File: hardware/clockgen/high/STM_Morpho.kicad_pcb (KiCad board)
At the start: 4 copper layers, 70 x 95.8 mm, 32 parts, among them CN10 Conn_02x19_Odd_Even, CN7 Conn_02x19_Odd_Even, J1 Conn_02x20_Odd_Even, J2 Conn_02x20_Odd_Even, U1 74ALVC164245DLG4, U10 CD40109BNSR, U2 74ALVC164245DLG4, U3 CD40109BNSR, U4 CD40109BNSR, U5 CD40109BNSR, U6 CD40109BNSR, U7 CD40109BNSR, U8 CD40109BNSR, U9 CD40109BNSR

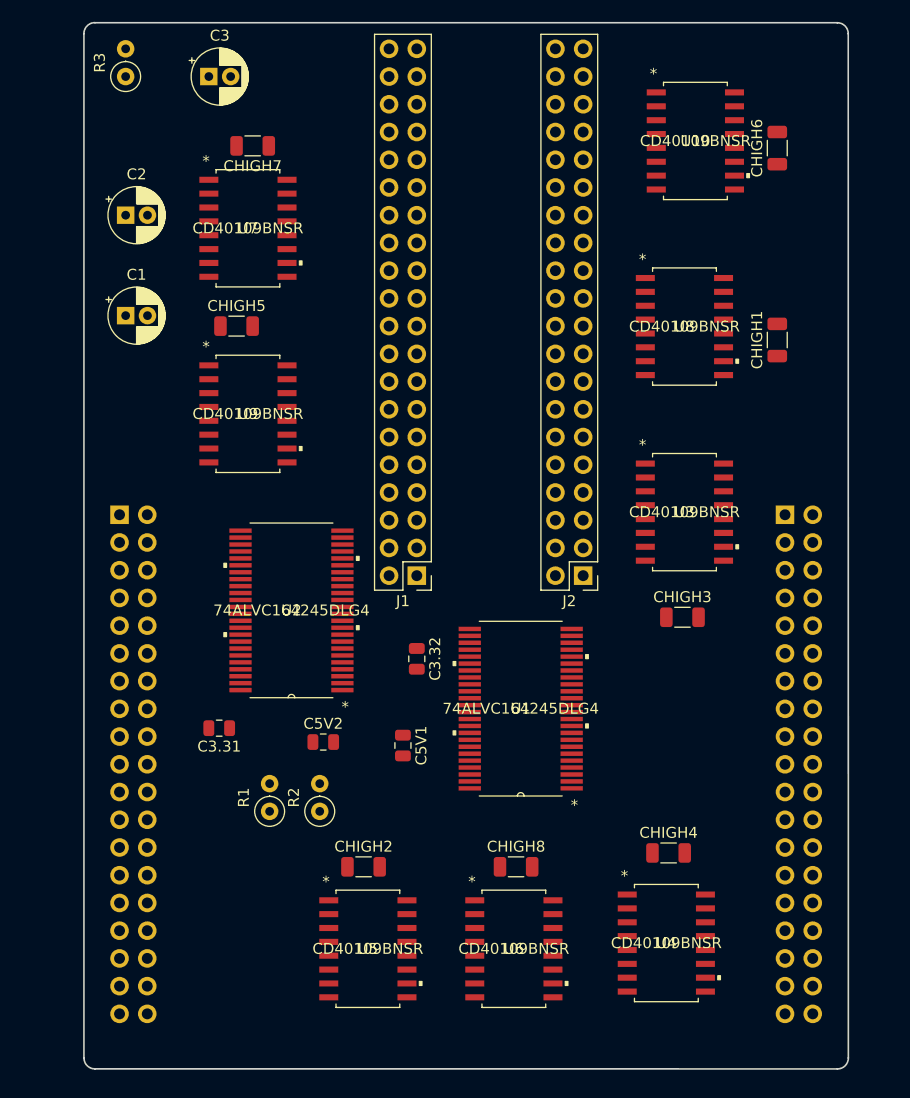
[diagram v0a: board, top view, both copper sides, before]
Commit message: Two PCBs are routed
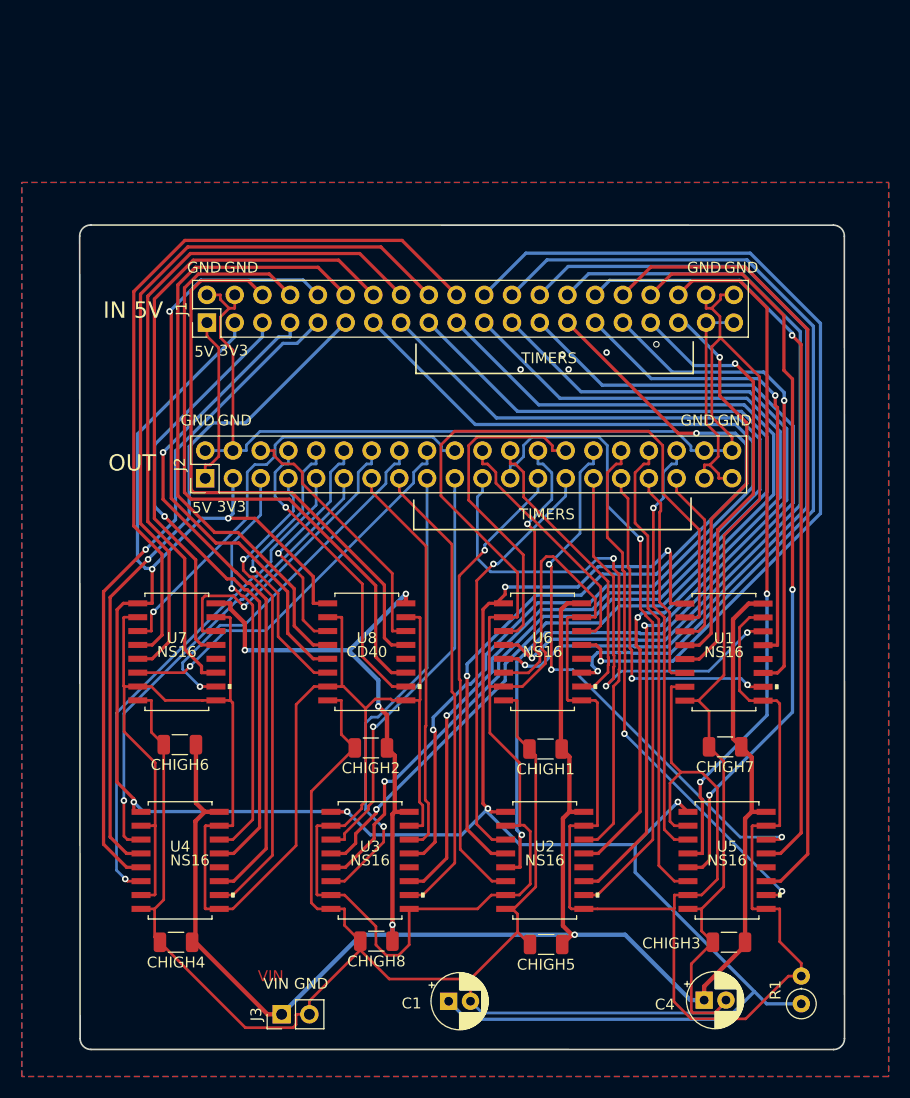
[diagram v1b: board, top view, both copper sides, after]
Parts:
- removed C2, C3: CP, Capacitor_THT:CP_Radial_D5.0mm_P2.00mm
- removed C3.31, C3.32, C5V1, C5V2: C, Capacitor_SMD:C_0805_2012Metric
- removed CN10, CN7: Conn_02x19_Odd_Even, Connector_PinSocket_2.54mm:PinSocket_2x19_P2.54mm_Vertical
- removed R2: 10K, Resistor_THT:R_Axial_DIN0207_L6.3mm_D2.5mm_P2.54mm_Vertical
- removed R3: 1K, Resistor_THT:R_Axial_DIN0207_L6.3mm_D2.5mm_P2.54mm_Vertical
- removed U10, U9: CD40109BNSR, CD40109BNSR:CD40109BNSR
- added C4: CP, Capacitor_THT:CP_Radial_D5.0mm_P2.00mm, F.Cu at (186.8, 115.7)
- added J3: Conn_01x02_Female, Connector_PinHeader_2.54mm:PinHeader_1x02_P2.54mm_Vertical, F.Cu at (148.1, 117.0)
- R1: value 10K -> 1K
- U1, U2: value 74ALVC164245DLG4 -> NS16; footprint footprints:74ALVC164245DLG4 -> CD40109BNSR:CD40109BNSR
- U3, U4, U5, U6, U7: value CD40109BNSR -> NS16
- U8: value CD40109BNSR -> CD40
- moved CHIGH6 77.3 mm to (138.8, 92.3), turned to 180 degrees
- moved CHIGH7 70.0 mm to (188.7, 92.5)
- moved C1 69.4 mm to (163.4, 115.8)
- moved CHIGH5 63.3 mm to (172.3, 110.6), turned to 180 degrees
- moved R1 51.8 mm to (195.7, 116.0)
- moved CHIGH4 45.9 mm to (138.4, 110.4), turned to 180 degrees
- moved U4 45.2 mm to (138.8, 102.9)
- moved CHIGH1 43.1 mm to (172.3, 92.7), turned to 180 degrees
- moved U3 43.0 mm to (156.2, 102.9)
- moved U8 41.7 mm to (155.9, 83.8)
- moved U7 39.3 mm to (138.5, 83.8)
- moved J2 35.8 mm to (141.1, 67.9), turned to 90 degrees
- moved U5 33.9 mm to (188.9, 102.9)
- moved U2 32.6 mm to (172.2, 102.9), turned to 0 degrees
- moved J1 30.1 mm to (141.3, 53.6), turned to 90 degrees
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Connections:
- C1 pad 1: +5V -> +3V3
- J1 pad 1: +5V -> /+5V
- J1 pad 10: /PB9_5V -> /PC8_HIGH
- J1 pad 11: /PA6_5V -> /PA3_HIGH
- J1 pad 12: /PA7_5V -> /PC6_HIGH
- J1 pad 13: /PA1_5V -> /PA2_HIGH
- J1 pad 14: /PA2_5V -> /PC5_HIGH
- J1 pad 15: /PA3_5V -> /PA1_HIGH
- J1 pad 16: /PA4_5V -> /PC4_HIGH
- J1 pad 17: /PA5_5V -> /PA7_HIGH
- J1 pad 18: /PA8_5V -> /PC3_HIGH
- J1 pad 19: /NC -> /PA6_HIGH
- J1 pad 2: +3V3 -> GND
- J1 pad 20: /NC -> /PC2_HIGH
- J1 pad 21: GND -> /PB9_HIGH
- J1 pad 22: GND -> /PC1_HIGH
- J1 pad 23: /PA9_5V -> /PB8_HIGH
- J1 pad 24: /PA11_5V -> /PC0_HIGH
- J1 pad 25: /PA12_5V -> /PC7_HIGH
- J1 pad 26: /PA13_5V -> /PA15_HIGH
- J1 pad 27: /PA14_5V -> /PA0_HIGH
- J1 pad 28: /PA15_5V -> /PA14_HIGH
- J1 pad 29: /PC0_5V -> /PB6_HIGH
- J1 pad 3: /PA10_5V -> +3V3
- J1 pad 30: /PC1_5V -> /PA13_HIGH
- J1 pad 31: /PC2_5V -> /PB5_HIGH
- J1 pad 32: /PC3_5V -> /PA12_HIGH
- J1 pad 33: /PC4_5V -> /PB10_HIGH
- J1 pad 34: /PC5_5V -> /PA11_HIGH
- J1 pad 35: /PC6_5V -> /PA10_HIGH
- J1 pad 36: /PC8_5V -> /PA9_HIGH
- J1 pad 37: /PC9_5V -> /NC
- J1 pad 38: /PC10_5V -> GND
- J1 pad 39: GND -> /NC
- J1 pad 4: /PB10_5V -> GND
- J1 pad 5: /PB5_5V -> /PA8_HIGH
- J1 pad 6: /PB6_5V -> /PC10_HIGH
- J1 pad 7: /PA0_5V -> /PA5_HIGH
- J1 pad 8: /PC7_5V -> /PC9_HIGH
- J1 pad 9: /PB8_5V -> /PA4_HIGH
- J2 pad 1: +5V -> /+5V
- J2 pad 10: /PB9_HIGH -> /PC8_5V
- J2 pad 11: /PA6_HIGH -> /PA3_5V
- J2 pad 12: /PA7_HIGH -> /PC6_5V
- J2 pad 13: /PA1_HIGH -> /PA2_5V
- J2 pad 14: /PA2_HIGH -> /PC5_5V
- J2 pad 15: /PA3_HIGH -> /PA1_5V
- J2 pad 16: /PA4_HIGH -> /PC4_5V
- J2 pad 17: /PA5_HIGH -> /PA7_5V
- J2 pad 18: /PA8_HIGH -> /PC3_5V
- J2 pad 19: +15V -> /PA6_5V
- J2 pad 2: +3V3 -> GND
- J2 pad 20: +15V -> /PC2_5V
- J2 pad 21: GND -> /PB9_5V
- J2 pad 22: GND -> /PC1_5V
- J2 pad 23: /PA9_HIGH -> /PB8_5V
- J2 pad 24: /PA11_HIGH -> /PC0_5V
- J2 pad 25: /PA12_HIGH -> /PC7_5V
- J2 pad 26: /PA13_HIGH -> /PA15_5V
- J2 pad 27: /PA14_HIGH -> /PA0_5V
- J2 pad 28: /PA15_HIGH -> /PA14_5V
- J2 pad 29: /PC0_HIGH -> /PB6_5V
- J2 pad 3: /PA10_HIGH -> +3V3
- J2 pad 30: /PC1_HIGH -> /PA13_5V
- J2 pad 31: /PC2_HIGH -> /PB5_5V
- J2 pad 32: /PC3_HIGH -> /PA12_5V
- J2 pad 33: /PC4_HIGH -> /PB10_5V
- J2 pad 34: /PC5_HIGH -> /PA11_5V
- J2 pad 35: /PC6_HIGH -> /PA10_5V
- J2 pad 36: /PC8_HIGH -> /PA9_5V
- J2 pad 37: /PC9_HIGH -> /NC
- J2 pad 38: /PC10_HIGH -> GND
- J2 pad 39: GND -> /NC
- J2 pad 4: /PB10_HIGH -> GND
- J2 pad 5: /PB5_HIGH -> /PA8_5V
- J2 pad 6: /PB6_HIGH -> /PC10_5V
- J2 pad 7: /PA0_HIGH -> /PA5_5V
- J2 pad 8: /PC7_HIGH -> /PC9_5V
- J2 pad 9: /PB8_HIGH -> /PA4_5V
- R1 pad 2: /PULLUP -> /PULLUP_HIGH
- U1 pad 1: /PULLUP -> +3V3
- U1 pad 10: GND -> /PB5_5V
- U1 pad 11: /PB8_5V -> /PB5_HIGH
- U1 pad 12: /PB9_5V -> (no net)
- U1 pad 13: /PA6_5V -> /PB6_HIGH
- U1 pad 14: /PA7_5V -> /PB6_5V
- U1 pad 15: GND -> /PULLUP_HIGH
- U1 pad 16: /PA1_5V -> +15V
- U1 pad 2: /PA10_5V -> /PULLUP_HIGH
- U1 pad 3: /PB10_5V -> /PA10_5V
- U1 pad 4: GND -> /PA10_HIGH
- U1 pad 5: /PB5_5V -> /PB10_HIGH
- U1 pad 6: /PB6_5V -> /PB10_5V
- U1 pad 7: +5V -> /PULLUP_HIGH
- U1 pad 8: /PA0_5V -> GND
- U1 pad 9: /PC7_5V -> /PULLUP_HIGH
- U2 pad 1: /PULLUP -> +3V3
- U2 pad 10: GND -> /PB8_5V
- U2 pad 11: /PC0_5V -> /PB8_HIGH
- U2 pad 12: /PC1_5V -> (no net)
- U2 pad 13: /PC2_5V -> /PB9_HIGH
- U2 pad 14: /PC3_5V -> /PB9_5V
- U2 pad 15: GND -> /PULLUP_HIGH
- U2 pad 16: /PC4_5V -> +15V
- U2 pad 2: /PA9_5V -> /PULLUP_HIGH
- U2 pad 3: /PA11_5V -> /PA0_5V
- U2 pad 4: GND -> /PA0_HIGH
- U2 pad 5: /PA12_5V -> /PC7_HIGH
- U2 pad 6: /PA13_5V -> /PC7_5V
- U2 pad 7: +5V -> /PULLUP_HIGH
- U2 pad 8: /PA14_5V -> GND
- U2 pad 9: /PA15_5V -> /PULLUP_HIGH
- U3 pad 10: /PB5 -> /PA1_5V
- U3 pad 11: /PB5_HIGH -> /PA1_HIGH
- U3 pad 13: /PB6_HIGH -> /PA2_HIGH
- U3 pad 14: /PB6 -> /PA2_5V
- U3 pad 3: /PA10 -> /PA6_5V
- U3 pad 4: /PA10_HIGH -> /PA6_HIGH
- U3 pad 5: /PB10_HIGH -> /PA7_HIGH
- U3 pad 6: /PB10 -> /PA7_5V
- U4 pad 10: /PB8 -> /PA5_5V
- U4 pad 11: /PB8_HIGH -> /PA5_HIGH
- U4 pad 13: /PB9_HIGH -> /PA8_HIGH
- U4 pad 14: /PB9 -> /PA8_5V
- U4 pad 3: /PA0 -> /PA3_5V
- U4 pad 4: /PA0_HIGH -> /PA3_HIGH
- U4 pad 5: /PC7_HIGH -> /PA4_HIGH
- U4 pad 6: /PC7 -> /PA4_5V
- U5 pad 10: /PA1 -> /PA12_5V
- U5 pad 11: /PA1_HIGH -> /PA12_HIGH
- U5 pad 13: /PA2_HIGH -> /PA13_HIGH
- U5 pad 14: /PA2 -> /PA13_5V
- U5 pad 3: /PA6 -> /PA9_5V
- U5 pad 4: /PA6_HIGH -> /PA9_HIGH
- U5 pad 5: /PA7_HIGH -> /PA11_HIGH
- U5 pad 6: /PA7 -> /PA11_5V
- U6 pad 10: /PA5 -> /PC0_5V
- U6 pad 11: /PA5_HIGH -> /PC0_HIGH
- U6 pad 13: /PA8_HIGH -> /PC1_HIGH
- U6 pad 14: /PA8 -> /PC1_5V
- U6 pad 3: /PA3 -> /PA14_5V
- U6 pad 4: /PA3_HIGH -> /PA14_HIGH
- U6 pad 5: /PA4_HIGH -> /PA15_HIGH
- U6 pad 6: /PA4 -> /PA15_5V
- U7 pad 10: /PA12 -> /PC4_5V
- U7 pad 11: /PA12_HIGH -> /PC4_HIGH
- U7 pad 13: /PA13_HIGH -> /PC5_HIGH
- U7 pad 14: /PA13 -> /PC5_5V
- U7 pad 3: /PA9 -> /PC2_5V
- U7 pad 4: /PA9_HIGH -> /PC2_HIGH
- U7 pad 5: /PA11_HIGH -> /PC3_HIGH
- U7 pad 6: /PA11 -> /PC3_5V
- U8 pad 10: /PC0 -> /PC9_5V
- U8 pad 11: /PC0_HIGH -> /PC9_HIGH
- U8 pad 13: /PC1_HIGH -> /PC10_HIGH
- U8 pad 14: /PC1 -> /PC10_5V
- U8 pad 3: /PA14 -> /PC6_5V
- U8 pad 4: /PA14_HIGH -> /PC6_HIGH
- U8 pad 5: /PA15_HIGH -> /PC8_HIGH
- U8 pad 6: /PA15 -> /PC8_5V
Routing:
- net /PULLUP_HIGH: track 0.00 -> 441.7 mm
- net GND: track 0.00 -> 313.8 mm, vias 0 -> 4
- net +3V3: track 0.00 -> 237.2 mm, vias 0 -> 8
- net +15V: track 0.00 -> 207.6 mm, vias 0 -> 5
- net /PA7_HIGH: track 0.00 -> 97.8 mm, vias 0 -> 1
- net /PA1_HIGH: track 0.00 -> 97.3 mm, vias 0 -> 1
- net /PA2_HIGH: track 0.00 -> 96.5 mm, vias 0 -> 1
- net /PA6_HIGH: track 0.00 -> 94.6 mm, vias 0 -> 1
- net /PC7_HIGH: track 0.00 -> 86.0 mm, vias 0 -> 1
- net /PC1_HIGH: track 0.00 -> 81.2 mm, vias 0 -> 1
- net /PB8_HIGH: track 0.00 -> 80.2 mm, vias 0 -> 1
- net /PB9_HIGH: track 0.00 -> 79.6 mm, vias 0 -> 1
- net /PA15_HIGH: track 0.00 -> 78.4 mm, vias 0 -> 1
- net /PC0_HIGH: track 0.00 -> 77.2 mm, vias 0 -> 1
- net /PA0_HIGH: track 0.00 -> 76.6 mm, vias 0 -> 2
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- added copper zone on B.Cu, net GND
- added copper zone on F.Cu, net GND
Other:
- board size 70 x 95.8 mm -> 70.1 x 75.5 mm
- copper layers 4 -> 2
- net class HighPower: trace_width 0.5 -> 0.4
- net class Power: trace_width 0.35 -> 0.3
- board text added: "3V3"
- board text added: "5V"
- board text added: "GND"
- board text added: "IN 5V"
- board text added: "OUT"
- board text added: "TIMERS"
- board text added: "VIN"

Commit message: Screw terminal adapter added
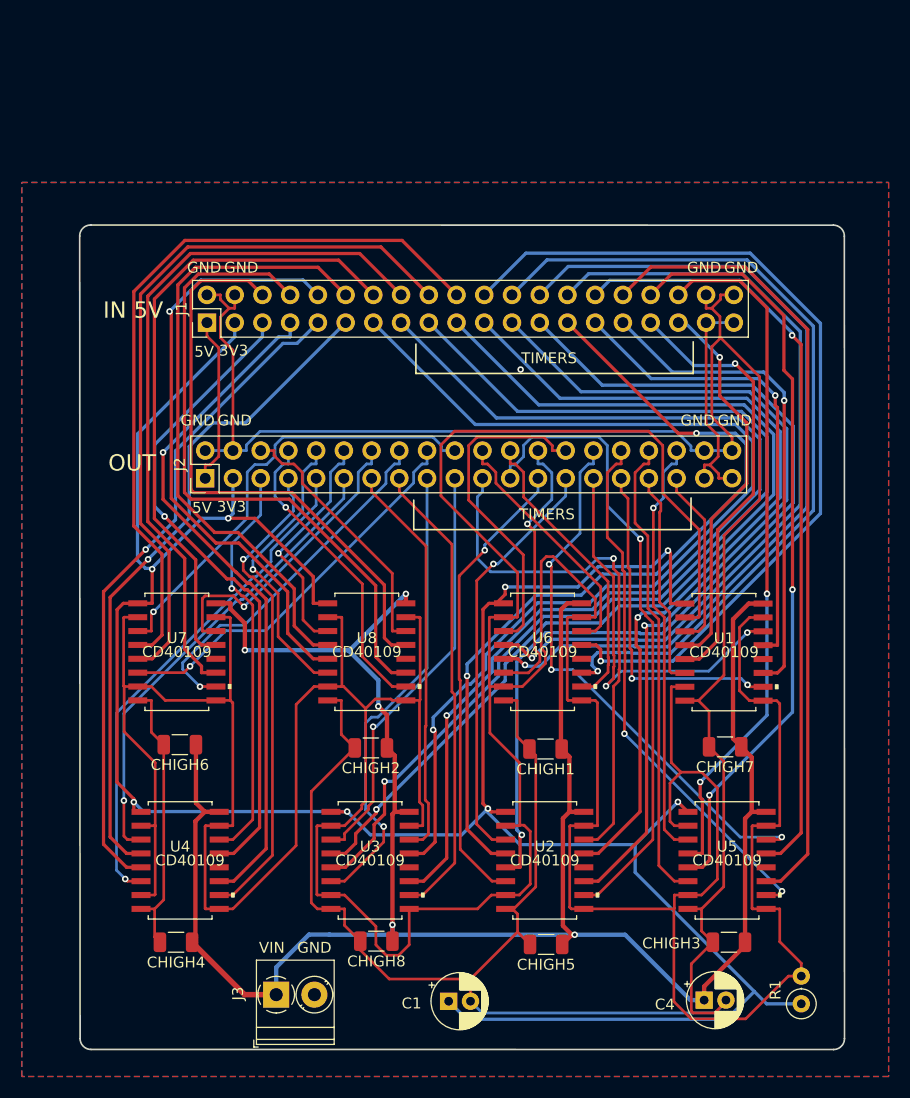
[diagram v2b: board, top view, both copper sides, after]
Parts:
- J3: footprint Connector_PinHeader_2.54mm:PinHeader_1x02_P2.54mm_Vertical -> TerminalBlock_Phoenix:TerminalBlock_Phoenix_PT-1,5-2-3.5-H_1x02_P3.50mm_Horizontal
- U1, U2, U3, U4, U5, U6, U7: value NS16 -> CD40109
- U8: value CD40 -> CD40109
- moved J3 1.87 mm to (147.6, 115.2), turned to 0 degrees
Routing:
- net GND: track 313.8 -> 288.0 mm, vias 4 -> 1
- net +15V: track 207.6 -> 208.4 mm
- net /PA14_5V: vias 1 -> 0
